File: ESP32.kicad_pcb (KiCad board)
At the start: 2 copper layers, 48 x 37 mm, 25 parts, among them J1 USB_B_Micro, J2 BATT, J3 PMS7003 Connector, J4 BootSel, J5 UART, SW1 RESET, U1 ESP32-C3-MINI-1, U2 AMS1117-3.3, U3 AMS1117-5.0

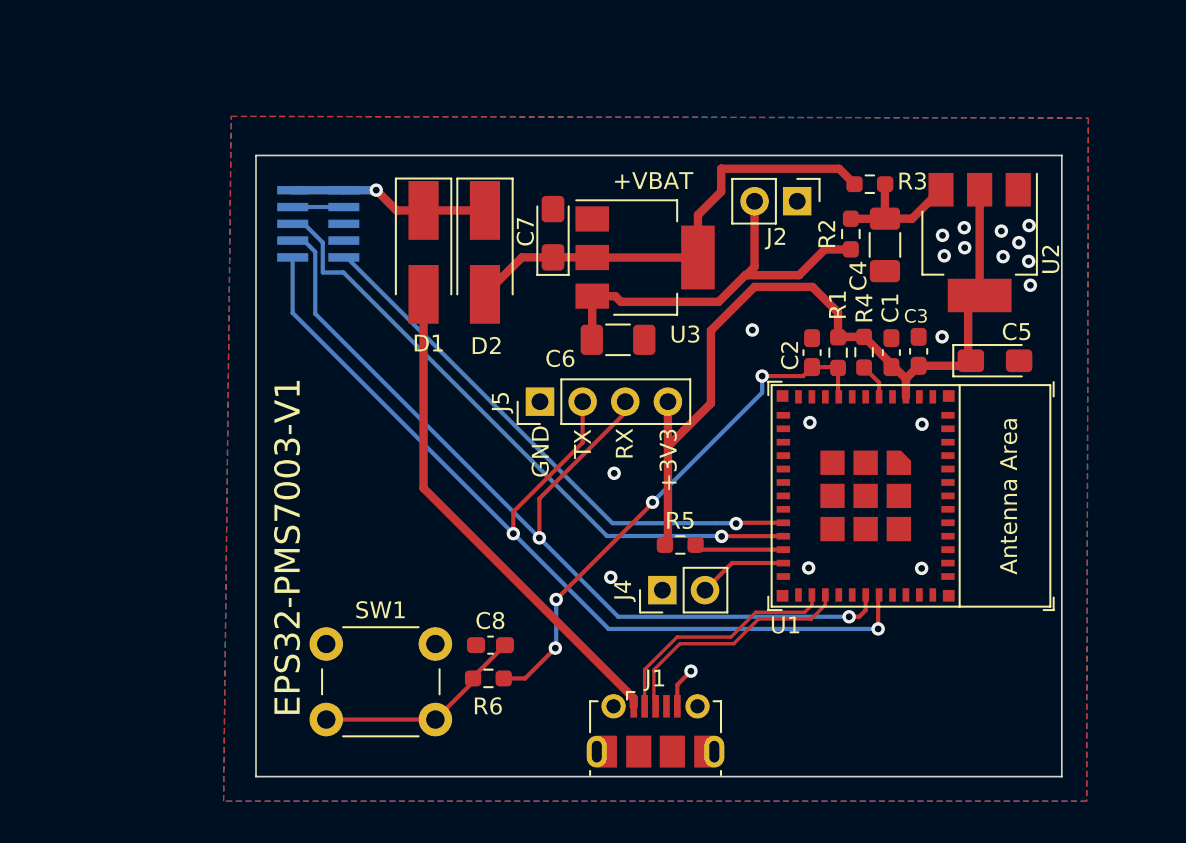
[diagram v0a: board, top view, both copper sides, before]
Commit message: Rework of power + PCB cleanup
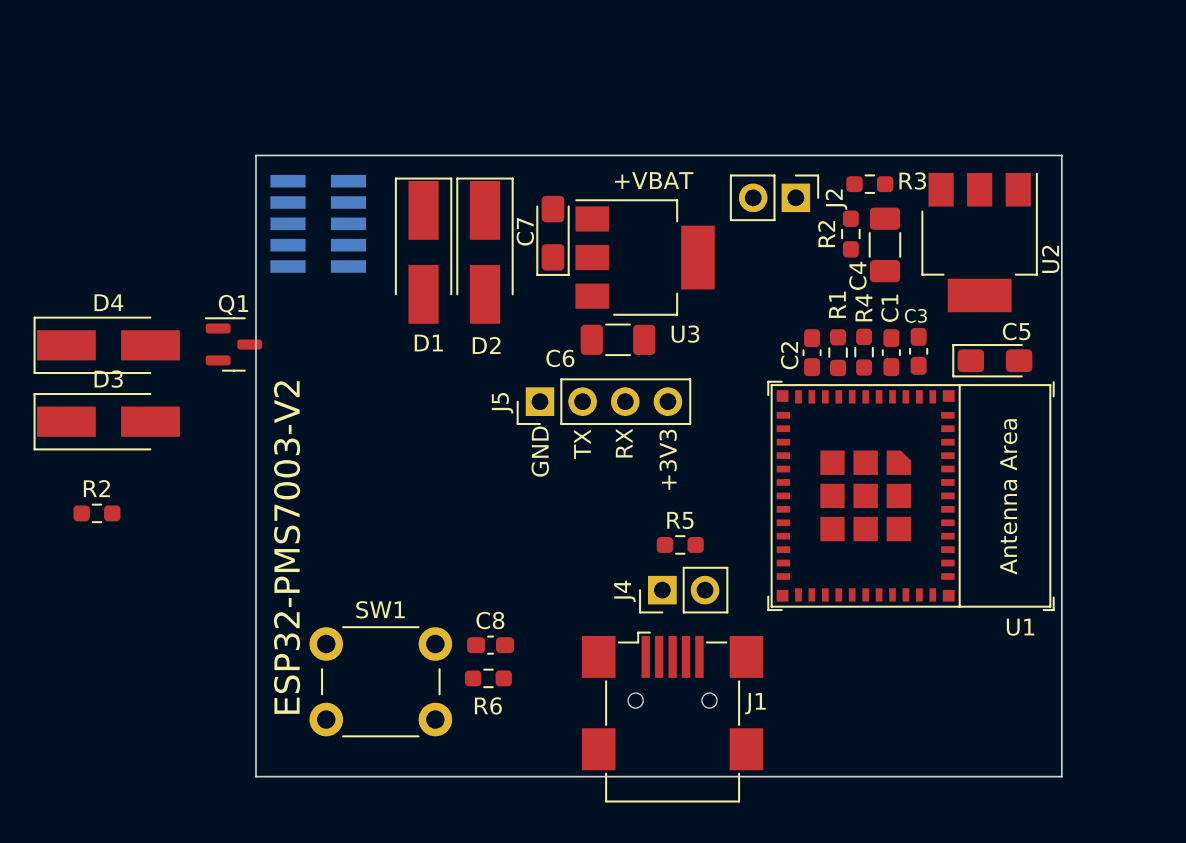
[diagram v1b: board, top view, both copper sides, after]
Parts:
- added D3: SS14, Diode_SMD:D_SMA_Handsoldering, F.Cu at (81.4, 76.3)
- added D4: SS14, Diode_SMD:D_SMA_Handsoldering, F.Cu at (81.4, 71.7)
- added Q1: AO3401A, Package_TO_SOT_SMD:SOT-23, F.Cu at (88.9, 71.7)
- added R2: 10k, Resistor_SMD:R_0603_1608Metric_Pad0.98x0.95mm_HandSolder, F.Cu at (80.7, 81.7)
- J1: footprint Connector_USB:USB_Micro-B_Molex-105017-0001 -> Connector_USB:USB_Mini-B_Wuerth_65100516121_Horizontal
- J3: footprint Connector_PinSocket_1.00mm:PinSocket_2x05_P1.00mm_Vertical_SMD -> Connector_PinSocket_1.27mm:PinSocket_2x05_P1.27mm_Vertical_SMD
- moved J1 2.07 mm to (115.0, 92.9)
- moved J2 0.22 mm to (122.4, 62.9)
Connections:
- C4 pad 1: /3v3_reg_vin -> Net-(C4-Pad1)
- C6 pad 1: /B+ -> Net-(C6-Pad1)
- C7 pad 1: /5v_reg_out -> Net-(C7-Pad1)
- D2 pad 2: /5v_reg_out -> Net-(C7-Pad1)
- J2 pad 2: /B+ -> +BATT
- R2 pad 1: /B+ -> VBAT
- R2 pad 2: /3v3_reg_vin -> /3v3_reg_in
- R3 pad 1: /5v_reg_out -> 5V_reg_out
- R3 pad 2: /3v3_reg_vin -> /3v3_reg_in
- U2 pad 3: /3v3_reg_vin -> Net-(C4-Pad1)
- U3 pad 2: /5v_reg_out -> Net-(C7-Pad1)
- U3 pad 3: /B+ -> Net-(C6-Pad1)
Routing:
- net PMS_RX: track 57.6 -> 0.00 mm, vias 2 -> 0
- net PMS_TX: track 57.0 -> 0.00 mm, vias 2 -> 0
- net +3V3: track 48.4 -> 0.00 mm
- net PMS_RST: track 38.0 -> 0.00 mm, vias 1 -> 0
- net PMS_SET: track 32.8 -> 0.00 mm, vias 1 -> 0
- net EN_DLY: track 31.6 -> 0.00 mm, vias 4 -> 0
- net VBUS: track 29.7 -> 0.00 mm
- net /5v_reg_out: track 27.8 -> 0.00 mm
- net /B+: track 24.1 -> 0.00 mm
- net /USB_D+: track 14.6 -> 0.00 mm
- net /USB_D-: track 14.3 -> 0.00 mm
- net Net-(C8-Pad2): track 12.6 -> 0.00 mm
- net +5V: track 12.0 -> 0.00 mm, vias 1 -> 0
- net /3v3_reg_vin: track 8.15 -> 0.00 mm
- net GND: track 5.48 -> 0.00 mm, vias 19 -> 0
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- removed copper zone on B.Cu, net GND
- removed copper zone on F.Cu, net GND
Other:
- board text added: "ESP32-PMS7003-V2"
- board text removed: "EPS32-PMS7003-V1"

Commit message: New layout routing
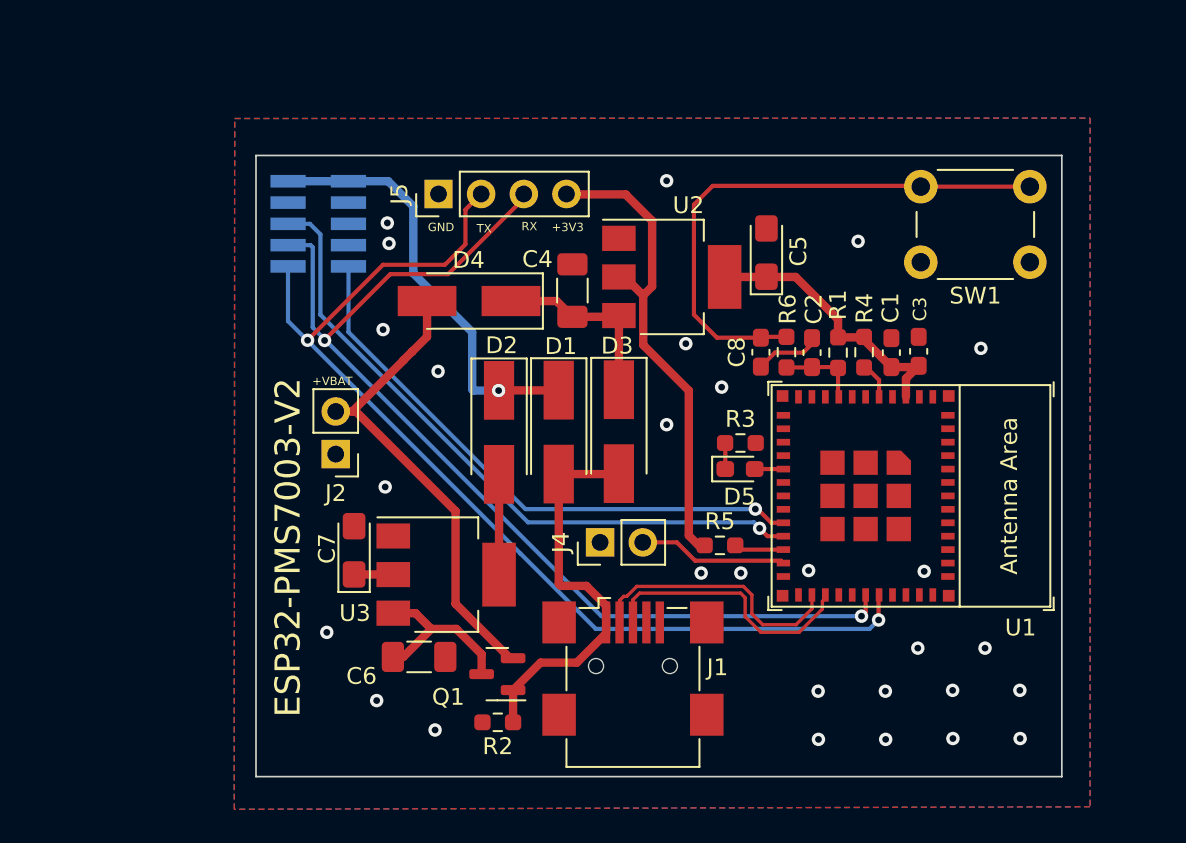
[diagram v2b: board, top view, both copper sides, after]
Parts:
- removed the R2 at (125.7, 65.1)
- added D5: GPIO10, LED_SMD:LED_0603_1608Metric_Pad1.05x0.95mm_HandSolder, F.Cu at (119.0, 79.1)
- R3: value 0 -> 220
- moved SW1 47.7 mm to (136.3, 66.8), turned to 180 degrees
- moved J2 31.4 mm to (95.0, 78.2), turned to 180 degrees
- moved D3 30.4 mm to (111.8, 76.9), turned to -90 degrees
- moved R2 26.9 mm to (104.6, 94.2), turned to 180 degrees
- moved R6 26.3 mm to (121.8, 72.1), turned to -90 degrees
- moved Q1 25.1 mm to (104.6, 91.3), turned to 180 degrees
- moved C8 23.7 mm to (120.3, 72.1), turned to 90 degrees
- moved C7 22.3 mm to (96.1, 83.9)
- moved C6 22.3 mm to (99.9, 90.3)
- moved U3 22.3 mm to (101.5, 85.4)
- moved D4 21.6 mm to (102.9, 69.1), turned to 180 degrees
- moved C4 18.8 mm to (109.1, 68.5), turned to 90 degrees
- moved U2 18.5 mm to (115.0, 67.7), turned to 0 degrees
- moved R3 17.2 mm to (119.1, 77.5)
- moved C5 15.1 mm to (120.6, 66.2), turned to 90 degrees
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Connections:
- net Net-(C4-Pad1) renamed /3v3RI
- net Net-(C6-Pad1) renamed /5vRI
- net Net-(C7-Pad1) renamed /5vRO
- R3 pad 1: 5V_reg_out -> Net-(D5-Pad1)
- R3 pad 2: /3v3_reg_in -> GND
- U1 pad 16: unconnected-(U1-Pad16) -> TEST_LED
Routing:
- net PMS_TX: track 0.00 -> 63.1 mm, vias 0 -> 2
- net PMS_RX: track 0.00 -> 62.9 mm, vias 0 -> 2
- net +3V3: track 0.00 -> 45.7 mm
- net PMS_RST: track 0.00 -> 40.0 mm, vias 0 -> 1
- net PMS_SET: track 0.00 -> 34.5 mm, vias 0 -> 1
- net Net-(C8-Pad2): track 0.00 -> 33.2 mm
- net +BATT: track 0.00 -> 29.3 mm
- net +5V: track 0.00 -> 25.6 mm, vias 0 -> 1
- net VBUS: track 0.00 -> 24.0 mm
- net /USB_D-: track 0.00 -> 15.9 mm
- net /USB_D+: track 0.00 -> 15.9 mm
- net /3v3RI: track 0.00 -> 11.3 mm
- net /5vRI: track 0.00 -> 10.4 mm
- net /BOOTSEL: track 0.00 -> 8.89 mm
- net /5vRO: track 0.00 -> 8.31 mm
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- added copper zone on B.Cu, net GND
- added copper zone on F.Cu, net GND

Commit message: Better power handling
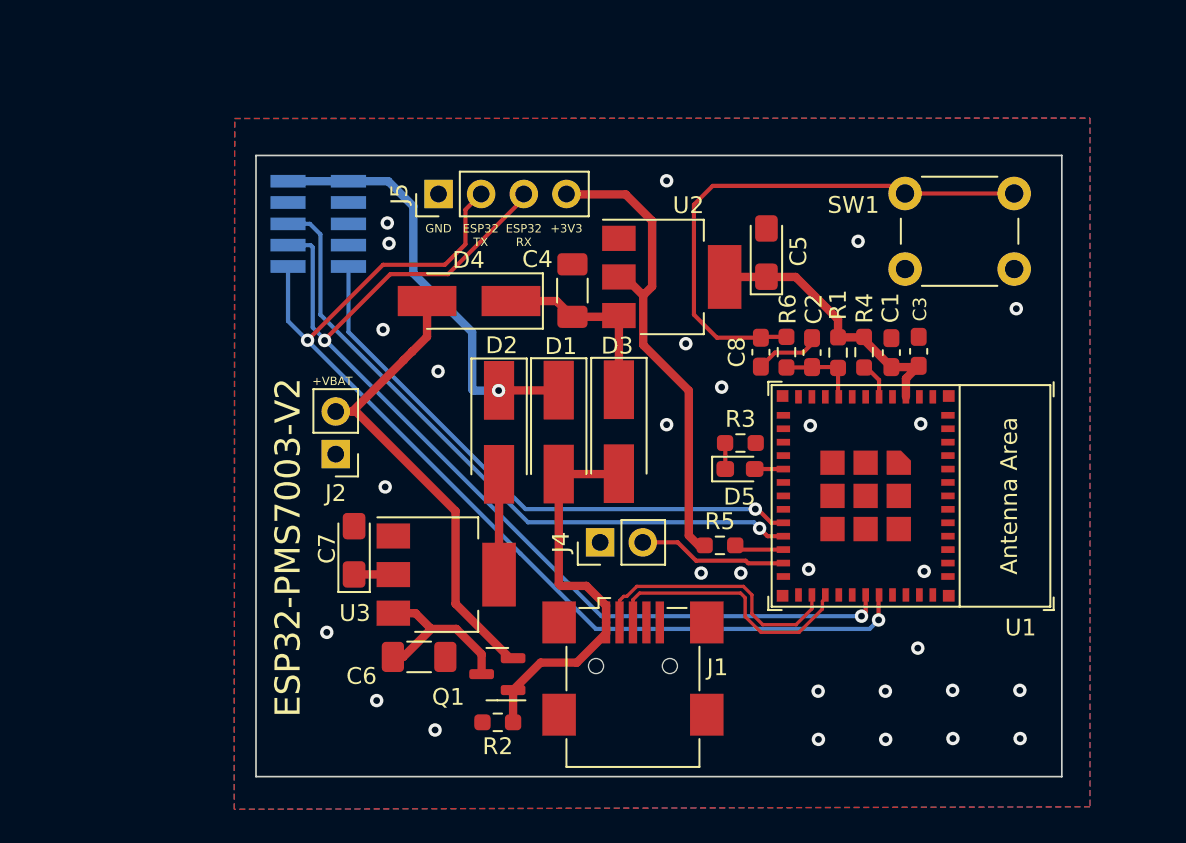
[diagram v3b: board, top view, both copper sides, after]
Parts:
- moved SW1 1.02 mm to (135.4, 67.2)
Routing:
- net Net-(C8-Pad2): track 33.2 -> 32.4 mm
- net GND: vias 28 -> 29
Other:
- board text added: "ESP32 RX"
- board text added: "ESP32 TX"
- board text removed: "RX"
- board text removed: "TX"

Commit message: Correct placement of the PMS header
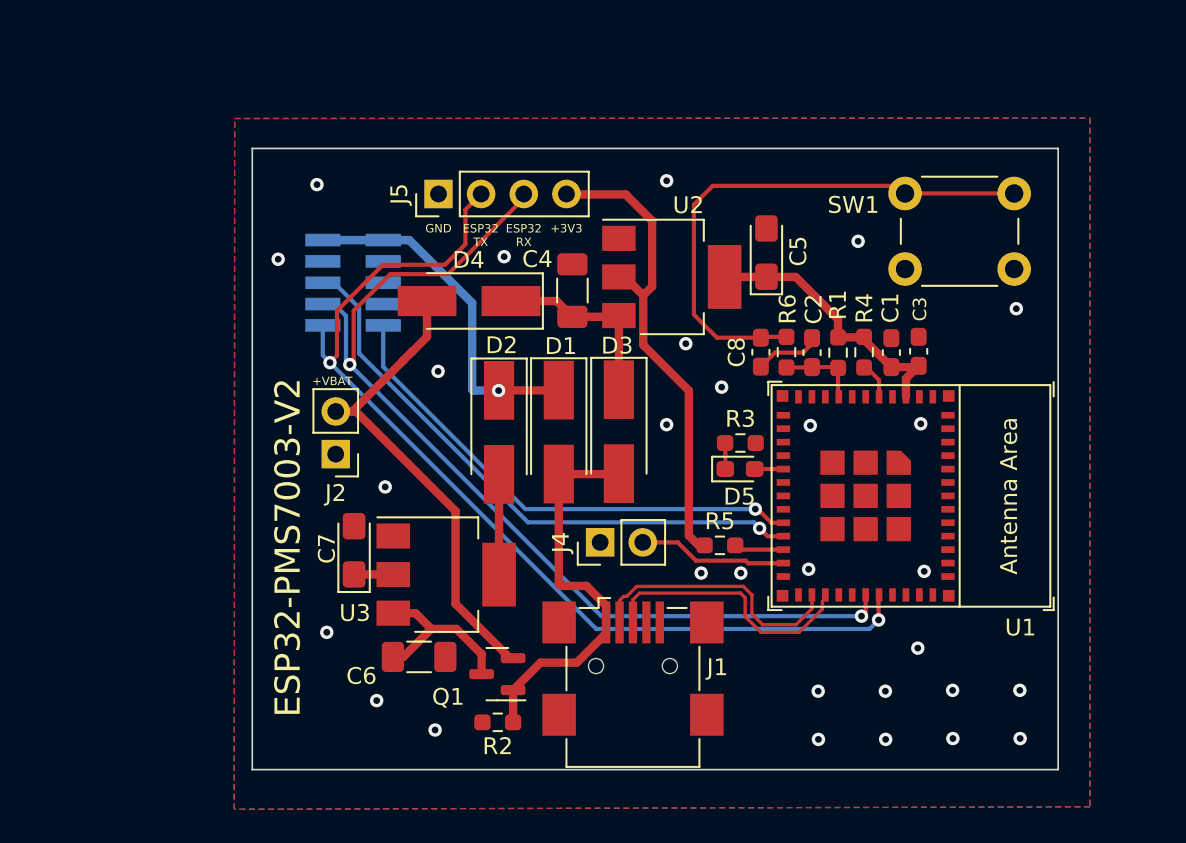
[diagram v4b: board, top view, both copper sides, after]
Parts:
- moved J3 4.07 mm to (96.0, 68.0)
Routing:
- net +5V: track 25.6 -> 20.8 mm
- net PMS_RST: track 40.0 -> 35.3 mm
- net PMS_SET: track 34.5 -> 30.2 mm
- net PMS_TX: track 63.1 -> 59.2 mm
- net PMS_RX: track 62.9 -> 59.3 mm

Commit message: Sch layout + reroute
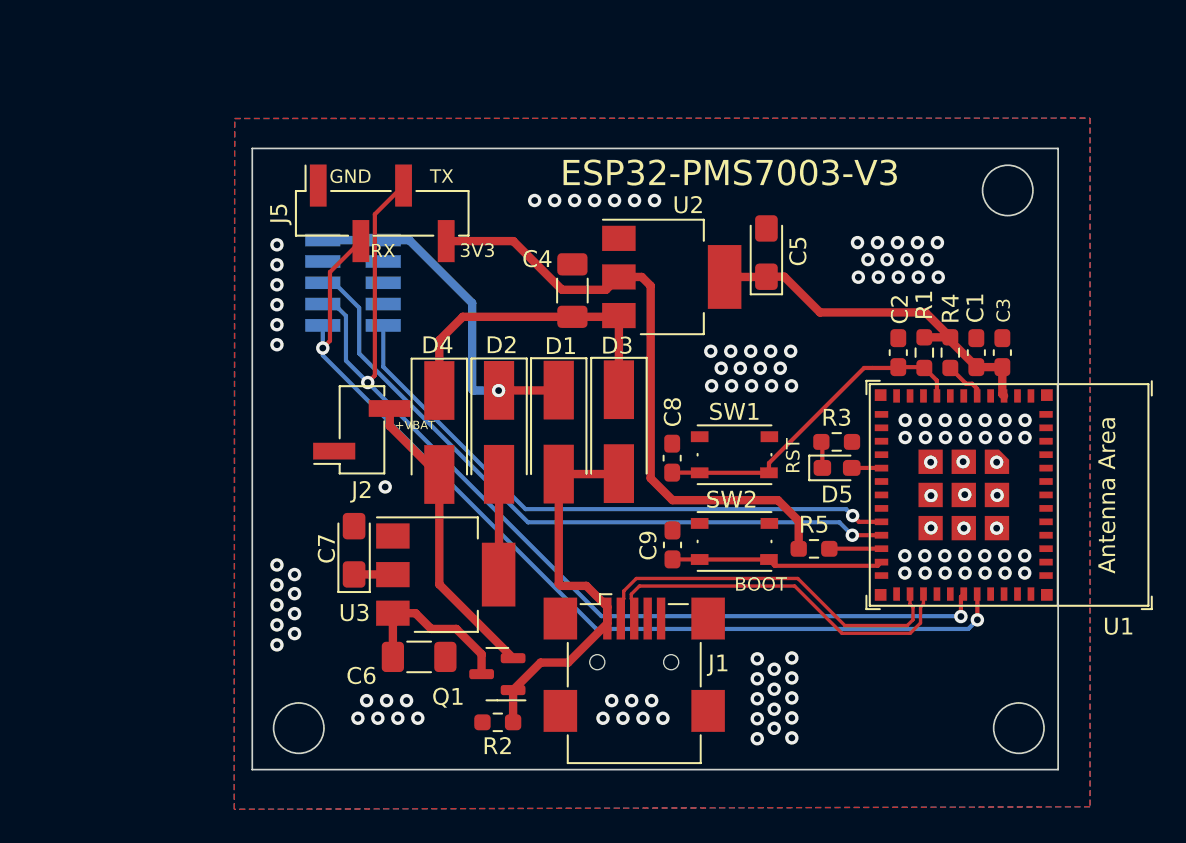
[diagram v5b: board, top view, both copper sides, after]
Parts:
- removed J4: BootSel, Connector_PinHeader_2.54mm:PinHeader_1x02_P2.54mm_Vertical
- removed R6: 0, Resistor_SMD:R_0603_1608Metric_Pad0.98x0.95mm_HandSolder
- added C9: 10u, Capacitor_SMD:C_0603_1608Metric_Pad1.08x0.95mm_HandSolder, F.Cu at (115.0, 83.6)
- added SW2: BOOTSEL, Button_Switch_SMD:SW_Push_1P1T_NO_Vertical_Wuerth_434133025816, F.Cu at (118.7, 83.4)
- J2: footprint Connector_PinHeader_2.54mm:PinHeader_1x02_P2.54mm_Vertical -> Connector_PinHeader_2.54mm:PinHeader_1x02_P2.54mm_Vertical_SMD_Pin1Right
- J5: footprint Connector_PinHeader_2.54mm:PinHeader_1x04_P2.54mm_Vertical -> Connector_PinHeader_2.54mm:PinHeader_1x04_P2.54mm_Vertical_SMD_Pin1Right
- SW1: footprint Button_Switch_THT:SW_PUSH_6mm -> Button_Switch_SMD:SW_Push_1P1T_NO_Vertical_Wuerth_434133025816
- moved SW1 20.0 mm to (118.7, 78.2), turned to 0 degrees
- moved C8 8.23 mm to (115.0, 78.4), turned to -90 degrees
- moved D4 8.03 mm to (101.1, 76.9), turned to -90 degrees
- moved U1 5.85 mm to (135.1, 80.6)
- moved D5 5.78 mm to (124.8, 79.0)
- moved R3 5.73 mm to (124.8, 77.5)
- moved R5 5.61 mm to (123.5, 83.8)
- moved R4 5.14 mm to (131.6, 72.2)
- moved R1 5.14 mm to (130.0, 72.2)
- moved C2 5.14 mm to (128.5, 72.2)
- moved C1 5.06 mm to (133.1, 72.2)
- moved C3 4.99 mm to (134.7, 72.2)
- moved J5 3.54 mm to (97.7, 63.9)
- moved J2 2.13 mm to (96.5, 76.8)
- moved J1 0.24 mm to (112.8, 90.6)
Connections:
- C8 pad 2: Net-(C8-Pad2) -> EN_DLY
- SW1 pad 2: Net-(C8-Pad2) -> EN_DLY
- U1 pad 23: /BOOTSEL -> BOOTSEL
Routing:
- net Net-(C8-Pad2): track 32.4 -> 0.00 mm
- net EN_DLY: track 4.84 -> 20.0 mm
- net +3V3: track 45.7 -> 59.3 mm
- net BOOTSEL: track 0.00 -> 12.7 mm
- net +BATT: track 29.3 -> 17.9 mm
- net /BOOTSEL: track 8.90 -> 0.00 mm
- net /3v3RI: track 11.3 -> 18.7 mm
- net /USB_D+: track 15.9 -> 22.2 mm
- net /USB_D-: track 15.9 -> 22.2 mm
- net PMS_SET: track 30.2 -> 36.0 mm
- net PMS_RST: track 35.3 -> 41.0 mm
- net GND: track 3.94 -> 0.04 mm, vias 29 -> 116
- net PMS_RX: track 59.3 -> 56.6 mm
- net PMS_TX: track 59.2 -> 61.3 mm
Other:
- outline, holes or cut-outs redrawn
- board text added: "3V3"
- board text added: "BOOT"
- board text added: "ESP32-PMS7003-V3"
- board text added: "RST"
- board text added: "RX"
- board text added: "TX"
- board text removed: "+3V3"
- board text removed: "ESP32 RX"
- board text removed: "ESP32 TX"
- board text removed: "ESP32-PMS7003-V2"
